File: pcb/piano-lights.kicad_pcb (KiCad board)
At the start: 2 copper layers, 98 x 48 mm, 49 parts, among them J1 FTDI RS232, J2 USB_B_Micro, J3 LED Strip, J4 AVR-ISP-6, J5 MIDI IN, J6 MIDI THRU, J7 MIDI Coupler Out, J8 MIDI Coupler In, SW1 Button, SW2 Reset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

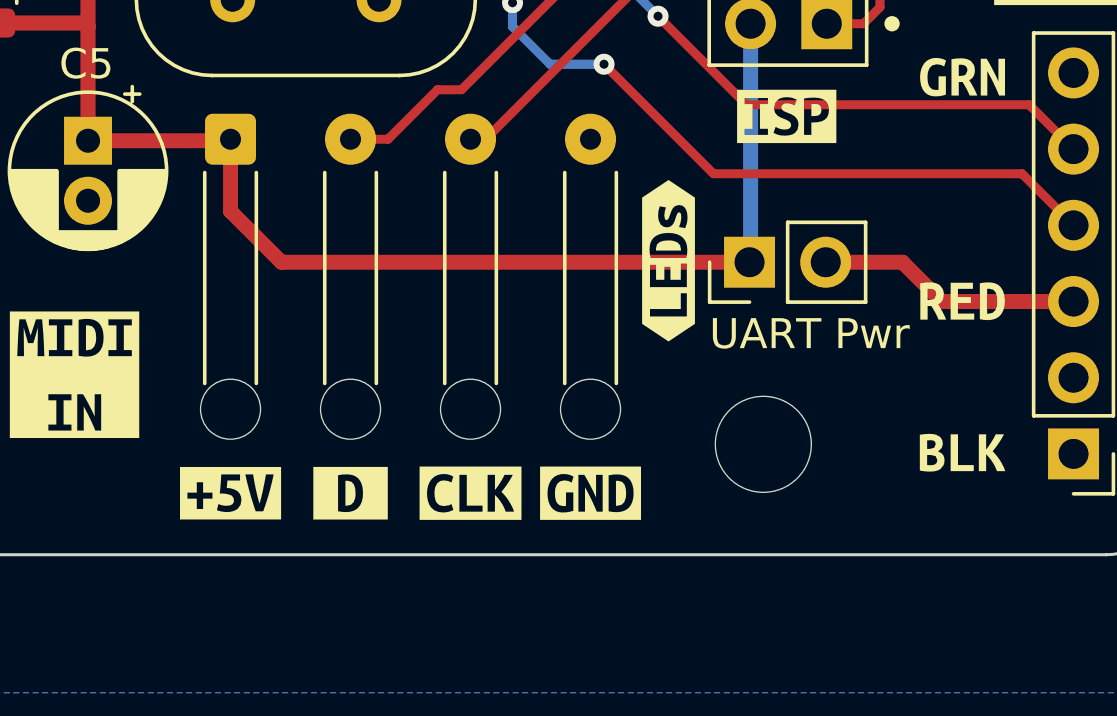
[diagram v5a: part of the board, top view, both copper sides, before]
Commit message: Update silkscreen for LED strip
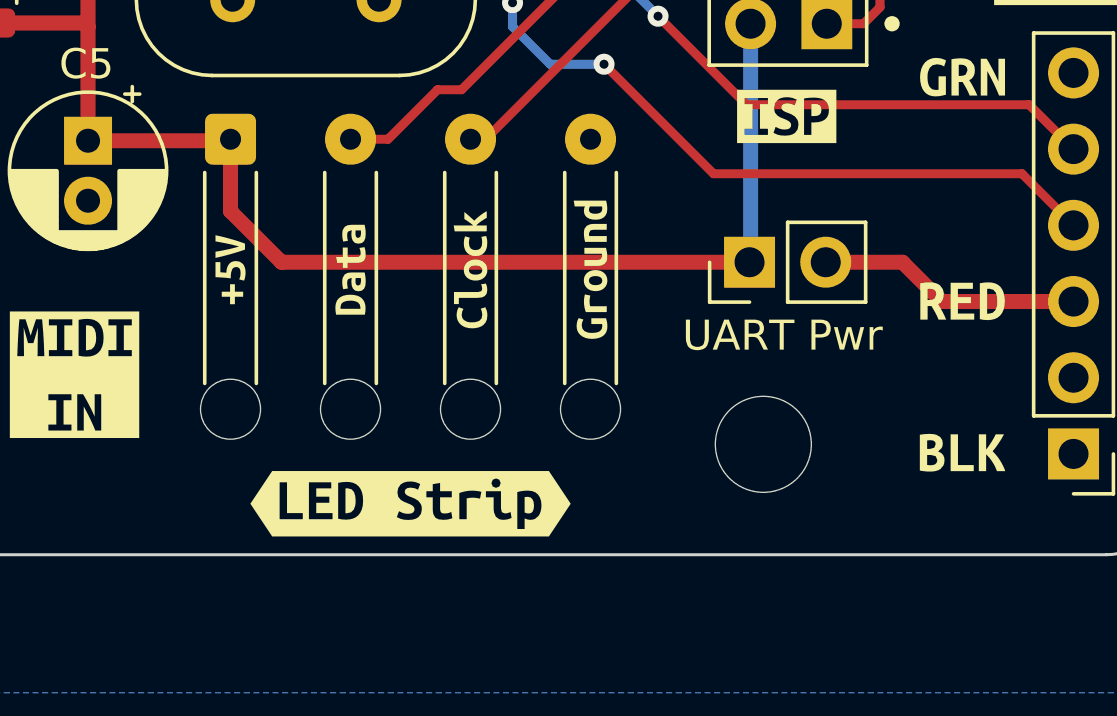
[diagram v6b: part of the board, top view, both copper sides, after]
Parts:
- removed kibuzzard-63E9D435: G***, kibuzzard-63E9D435
- removed kibuzzard-63E9D44E: G***, kibuzzard-63E9D44E
- removed kibuzzard-63E9D473: G***, kibuzzard-63E9D473
- removed kibuzzard-63E9D50C: G***, kibuzzard-63E9D50C
- removed kibuzzard-63E9D543: G***, kibuzzard-63E9D543
- added kibuzzard-63EAA92A: G***, kibuzzard-63EAA92A, F.Cu at (153.2, 105.5)
- added kibuzzard-63EAA932: G***, kibuzzard-63EAA932, F.Cu at (157.2, 105.5)
- added kibuzzard-63EAA93A: G***, kibuzzard-63EAA93A, F.Cu at (161.2, 105.5)
- added kibuzzard-63EAA942: G***, kibuzzard-63EAA942, F.Cu at (165.2, 105.5)
- added kibuzzard-63EAA95F: G***, kibuzzard-63EAA95F, F.Cu at (159.2, 113.3)

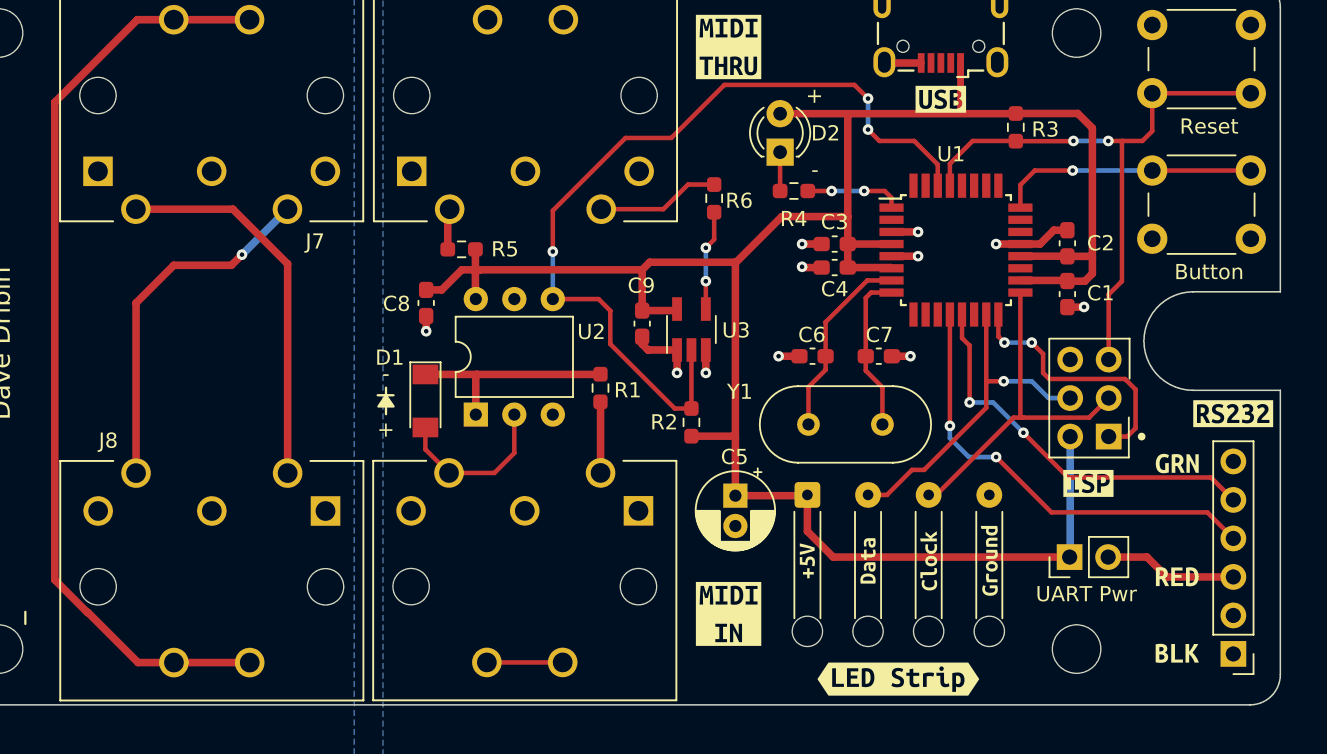
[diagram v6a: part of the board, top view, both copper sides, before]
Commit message: Add silkscreen for all RS323/FTDI pins
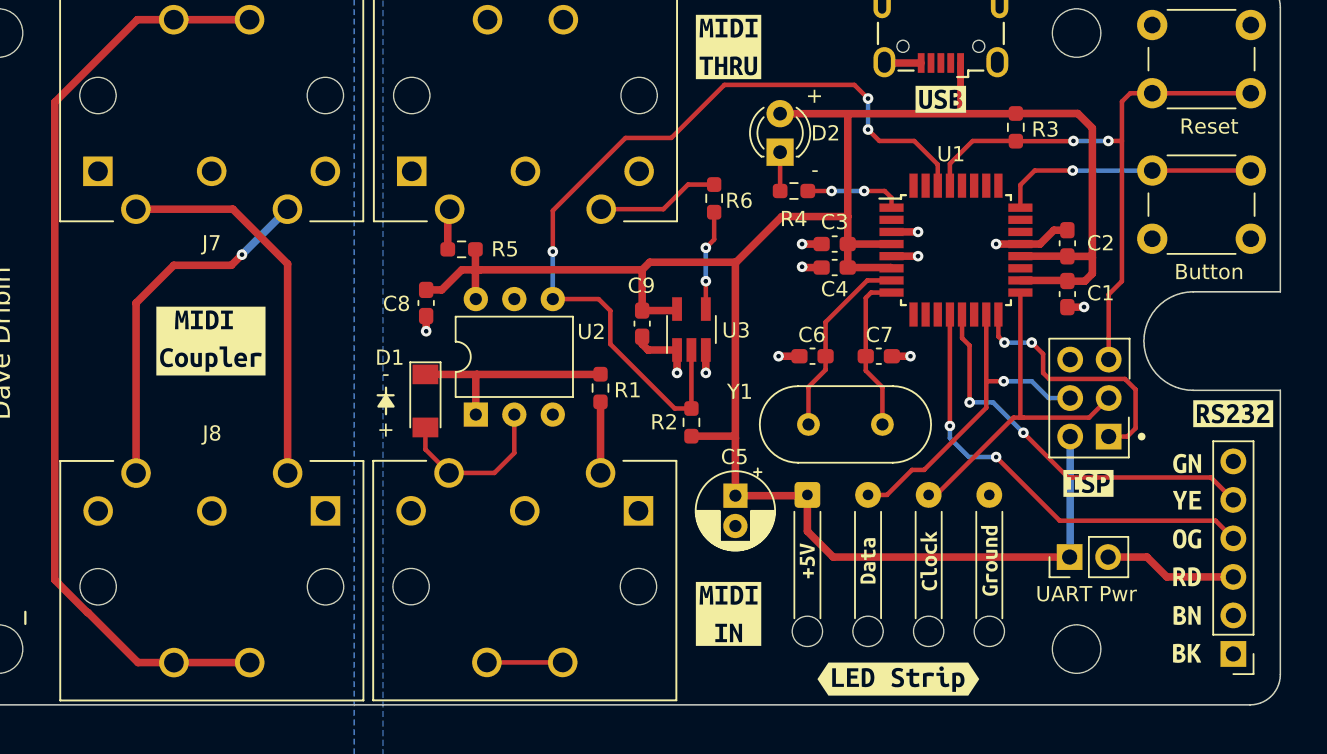
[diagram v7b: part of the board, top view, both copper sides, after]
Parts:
- removed kibuzzard-63E9D28E: G***, kibuzzard-63E9D28E
- removed kibuzzard-63E9D296: G***, kibuzzard-63E9D296
- removed kibuzzard-63EA7125: G***, kibuzzard-63EA7125
- added kibuzzard-63EAB850: G***, kibuzzard-63EAB850, F.Cu at (178.2, 111.6)
- added kibuzzard-63EAB855: G***, kibuzzard-63EAB855, F.Cu at (178.2, 99.1)
- added kibuzzard-63EAB85B: G***, kibuzzard-63EAB85B, F.Cu at (178.2, 106.5)
- added kibuzzard-63EAB86C: G***, kibuzzard-63EAB86C, F.Cu at (178.2, 101.5)
- added kibuzzard-63EAB881: G***, kibuzzard-63EAB881, F.Cu at (178.2, 104.0)
- added kibuzzard-63EAB895: G***, kibuzzard-63EAB895, F.Cu at (178.2, 109.1)
- added kibuzzard-63EAB91B: G***, kibuzzard-63EAB91B, F.Cu at (113.8, 91.0)

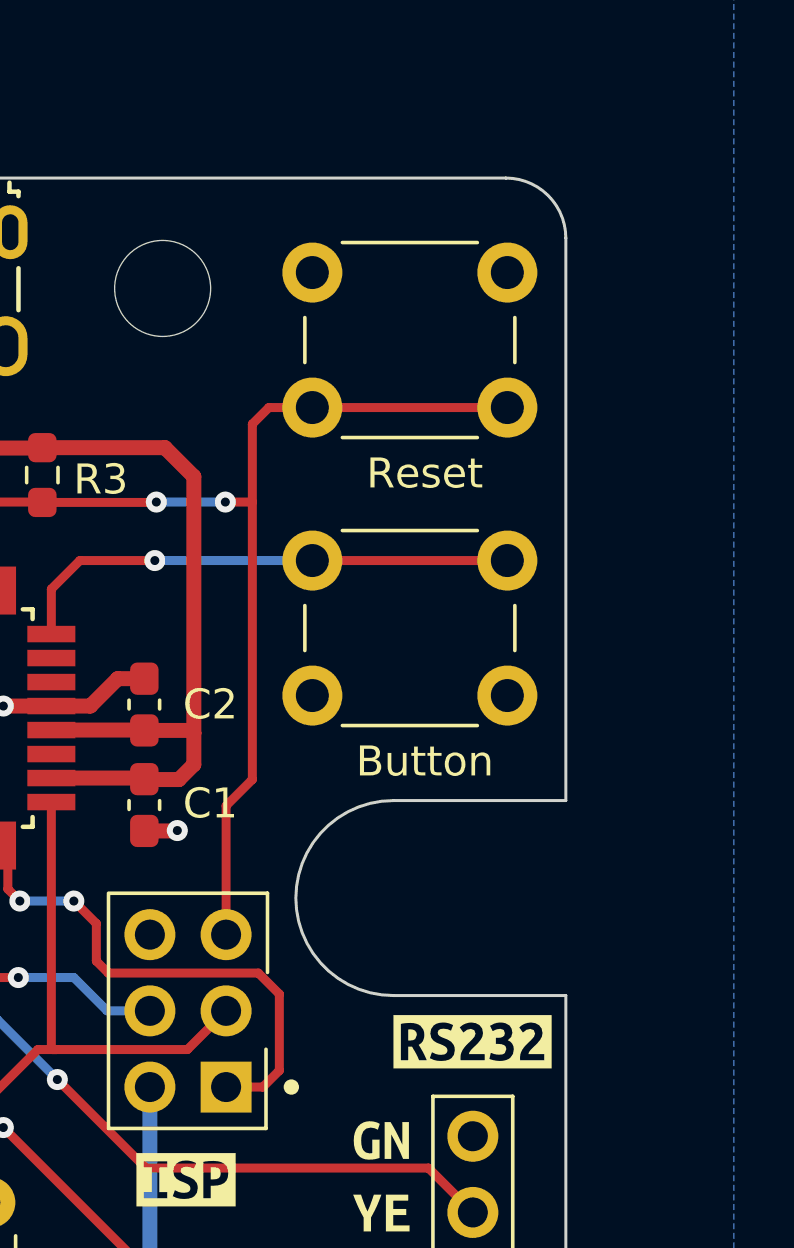
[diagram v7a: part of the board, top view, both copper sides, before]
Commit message: More siklscreen tweaks
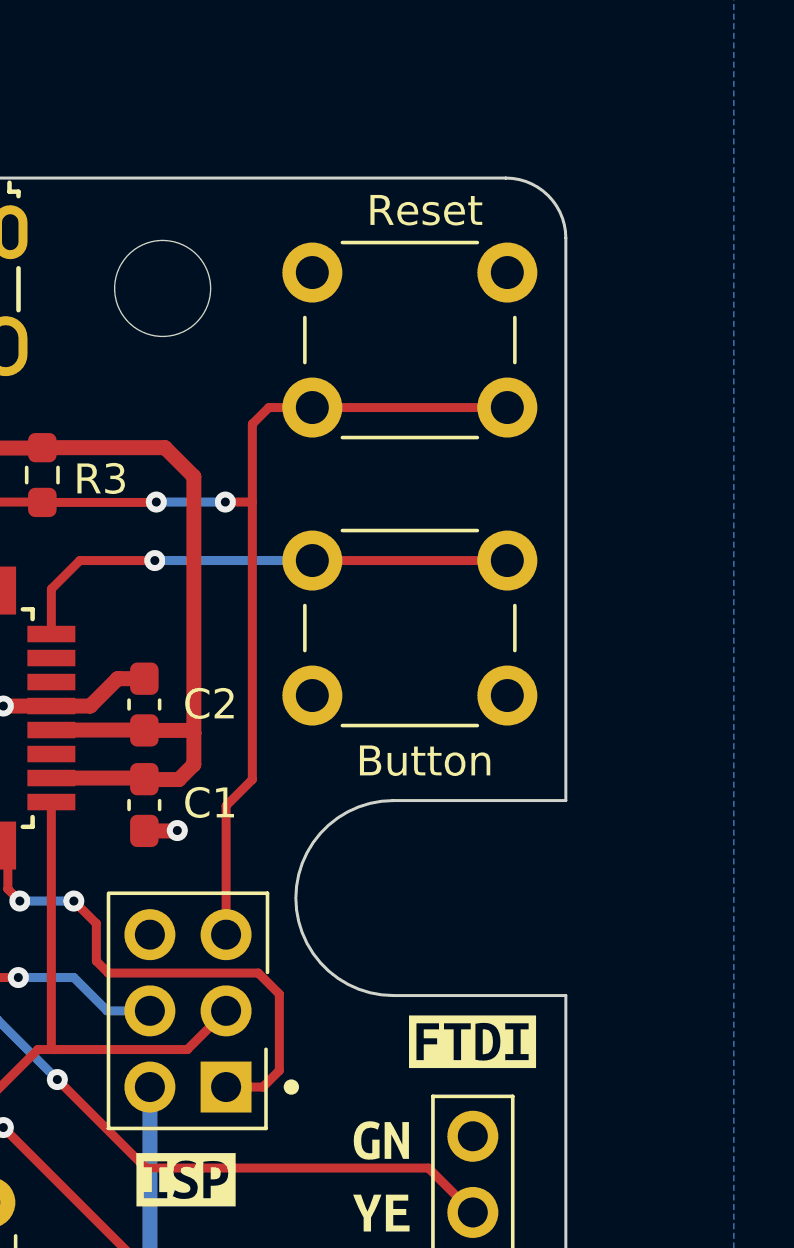
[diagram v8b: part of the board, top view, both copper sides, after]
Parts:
- removed kibuzzard-63E9D20D: G***, kibuzzard-63E9D20D
- added kibuzzard-63EABA39: G***, kibuzzard-63EABA39, F.Cu at (181.3, 95.8)
